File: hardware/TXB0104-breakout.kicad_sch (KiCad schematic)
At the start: 5 parts, among them J1 Conn_01x07_Male, J2 Conn_01x07_Male, U1 TXB0104D

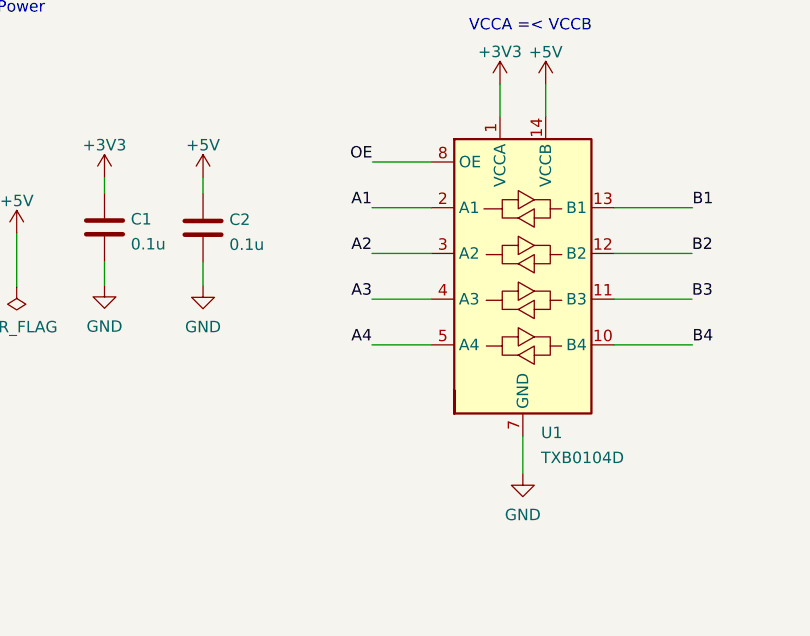
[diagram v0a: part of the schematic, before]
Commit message: Update board
- add pull down resistor to output enable pin to ensure off state during
  power on
- remove extra gound planes from the signal layer to reduce potential RF
  emissions from the board
- fix bottom silk screen
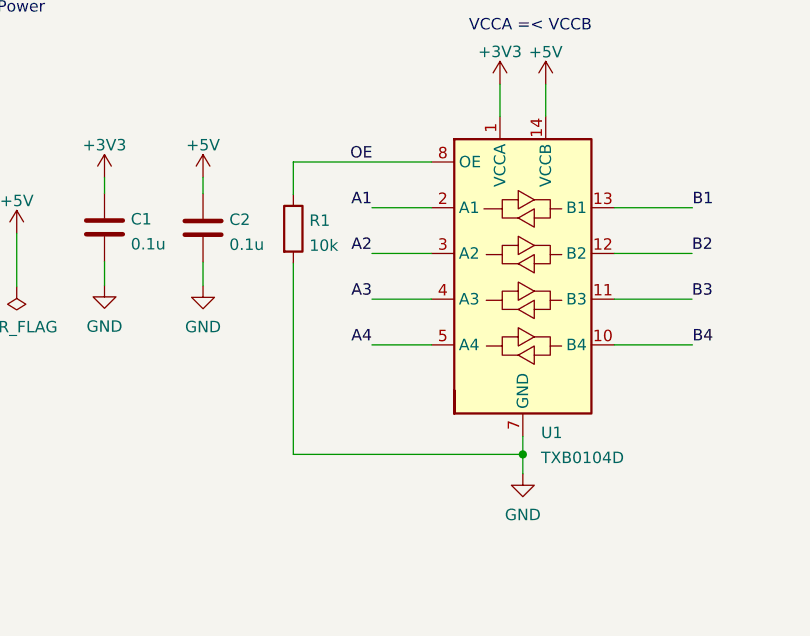
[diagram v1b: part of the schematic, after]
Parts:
- added R1: 10k, Resistor_SMD:R_0805_2012Metric_Pad1.20x1.40mm_HandSolder, symbol Device:R
- C1, C2: footprint Capacitor_SMD:C_0805_2012Metric -> Capacitor_SMD:C_0805_2012Metric_Pad1.18x1.45mm_HandSolder
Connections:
- net GND: now also R1.2
- net OE: now also R1.1
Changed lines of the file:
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@@
     (title "TXB0104-breakout")
     (date "2022-01-22")
-    (rev "1.0")
+    (rev "1.1")
     (company "sinustrom.info")
     (comment 1 "https://github.com/zpuskas/TXB0104-breakout")
@@
     (comment 3 "Bidirectional Voltage-level Translator With Automatic Direction Sensing")
   )
+  (junction (at 95.3516 90.0938) (diameter 0) (color 0 0 0 0)
+  )
   (no_connect (at 175.9712 75.2856))
   (no_connect (at 144.9324 75.3364))
@@
     (stroke (width 0) (type default) (color 0 0 0 0))
   )
-  (wire (pts (xy 95.3516 92.2528) (xy 95.3516 88.0872))
+  (wire (pts (xy 95.3516 92.2528) (xy 95.3516 90.0938))
     (stroke (width 0) (type default) (color 0 0 0 0))
   )
@@
     (stroke (width 0) (type default) (color 0 0 0 0))
   )
+  (wire (pts (xy 95.3516 90.0938) (xy 69.85 90.0938))
+    (stroke (width 0) (type default) (color 0 0 0 0))
+  )
   (wire (pts (xy 20.828 65.405) (xy 20.828 71.247))
     (stroke (width 0) (type default) (color 0 0 0 0))
@@
     (stroke (width 0) (type default) (color 0 0 0 0))
   )
+  (wire (pts (xy 95.3516 90.0938) (xy 95.3516 88.0872))
+    (stroke (width 0) (type default) (color 0 0 0 0))
+  )
+  (wire (pts (xy 69.85 57.6072) (xy 69.85 61.214))
+    (stroke (width 0) (type default) (color 0 0 0 0))
+  )
   (wire (pts (xy 167.7416 62.5856) (xy 175.9712 62.5856))
     (stroke (width 0) (type default) (color 0 0 0 0))
@@
     (stroke (width 0) (type default) (color 0 0 0 0))
   )
-  (wire (pts (xy 78.6384 57.6072) (xy 85.1916 57.6072))
+  (wire (pts (xy 69.85 57.6072) (xy 85.1916 57.6072))
+    (stroke (width 0) (type default) (color 0 0 0 0))
+  )
+  (wire (pts (xy 69.85 68.834) (xy 69.85 90.0938))
     (stroke (width 0) (type default) (color 0 0 0 0))
   )
@@
   (label "A3" (at 152.4 70.2564 0)
     (effects (font (size 1.27 1.27)) (justify left bottom))
+  )
+  (symbol (lib_id "Device:R") (at 69.85 65.024 0) (unit 1)
+    (in_bom yes) (on_board yes) (fields_autoplaced)
+    (property "Reference" "R1" (id 0) (at 71.628 64.1155 0)
+      (effects (font (size 1.27 1.27)) (justify left))
+    )
+    (property "Value" "10k" (id 1) (at 71.628 66.8906 0)
+      (effects (font (size 1.27 1.27)) (justify left))
+    )
+    (property "Footprint" "Resistor_SMD:R_0805_2012Metric_Pad1.20x1.40mm_HandSolder" (id 2) (at 68.072 65.024 90)
+      (effects (font (size 1.27 1.27)) hide)
+    )
+    (property "Datasheet" "~" (id 3) (at 69.85 65.024 0)
+      (effects (font (size 1.27 1.27)) hide)
+    )
+    (pin "1")
+    (pin "2")
   )
   (symbol (lib_id "power:+3V3") (at 48.8696 59.3344 0) (unit 1)
@@
       (effects (font (size 1.27 1.27)) (justify left))
     )
-    (property "Footprint" "Capacitor_SMD:C_0805_2012Metric" (id 2) (at 60.7822 68.7324 0)
+    (property "Footprint" "Capacitor_SMD:C_0805_2012Metric_Pad1.18x1.45mm_HandSolder" (id 2) (at 60.7822 68.7324 0)
       (effects (font (size 1.27 1.27)) hide)
     )
@@
       (effects (font (size 1.27 1.27)) (justify left))
     )
-    (property "Footprint" "Capacitor_SMD:C_0805_2012Metric" (id 2) (at 49.8348 68.6816 0)
+    (property "Footprint" "Capacitor_SMD:C_0805_2012Metric_Pad1.18x1.45mm_HandSolder" (id 2) (at 49.8348 68.6816 0)
       (effects (font (size 1.27 1.27)) hide)
     )
@@
     )
     (path "/9dc480ad-af3f-41d6-9cd0-6169d70e25bc"
-      (reference "C1") (unit 1) (value "0.1u") (footprint "Capacitor_SMD:C_0805_2012Metric")
+      (reference "C1") (unit 1) (value "0.1u") (footprint "Capacitor_SMD:C_0805_2012Metric_Pad1.18x1.45mm_HandSolder")
     )
     (path "/15aa31e9-b379-4d16-9236-d543913835f6"
-      (reference "C2") (unit 1) (value "0.1u") (footprint "Capacitor_SMD:C_0805_2012Metric")
+      (reference "C2") (unit 1) (value "0.1u") (footprint "Capacitor_SMD:C_0805_2012Metric_Pad1.18x1.45mm_HandSolder")
     )
     (path "/d65d7dc9-258b-4762-afad-18b66e2c9a6a"
@@
       (reference "J2") (unit 1) (value "Conn_01x07_Male") (footprint "Connector_PinHeader_2.54mm:PinHeader_1x07_P2.54mm_Vertical")
     )
+    (path "/09ab0b5c-3dee-42c8-b9e5-de0673874ccd"
+      (reference "R1") (unit 1) (value "10k") (footprint "Resistor_SMD:R_0805_2012Metric_Pad1.20x1.40mm_HandSolder")
+    )
     (path "/c8af5c52-f33f-499e-9f74-77425f3f2964"
